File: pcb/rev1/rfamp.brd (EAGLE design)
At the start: 40 x 20 mm, 17 parts, among them IC1 TS520530, IC2 ADL5523, X1 SAW-B3721

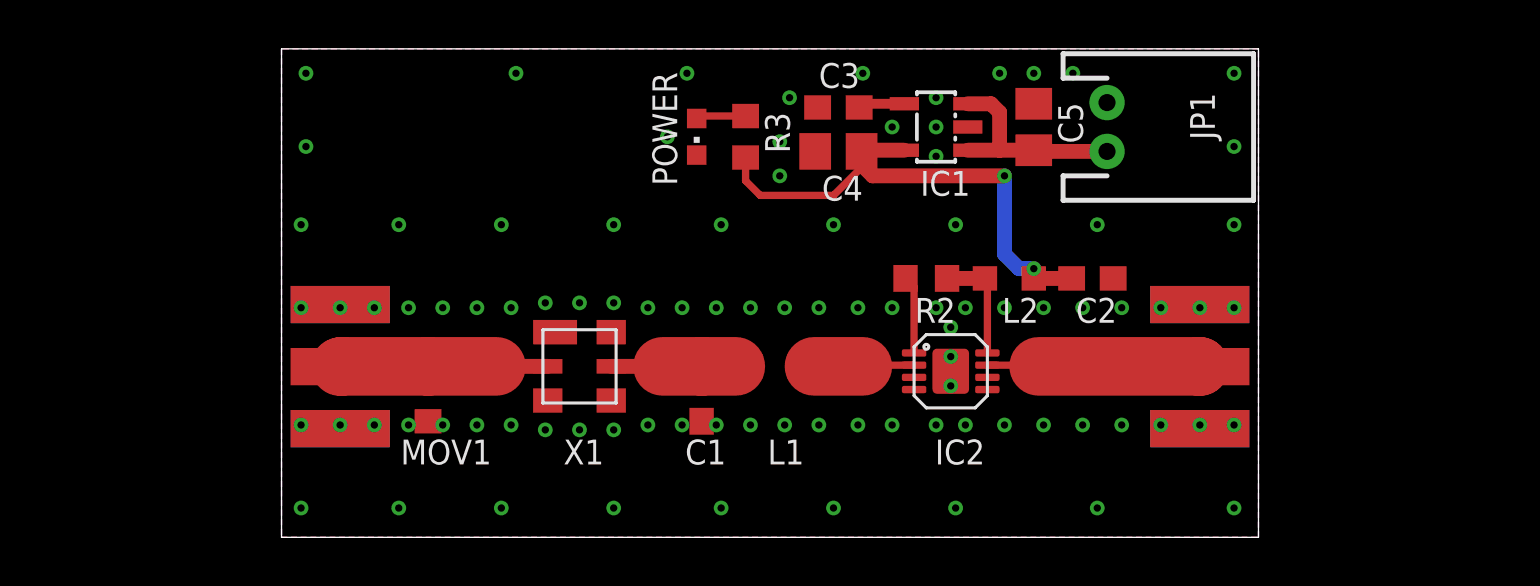
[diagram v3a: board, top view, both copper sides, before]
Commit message: Insert dc blocking capacitors.
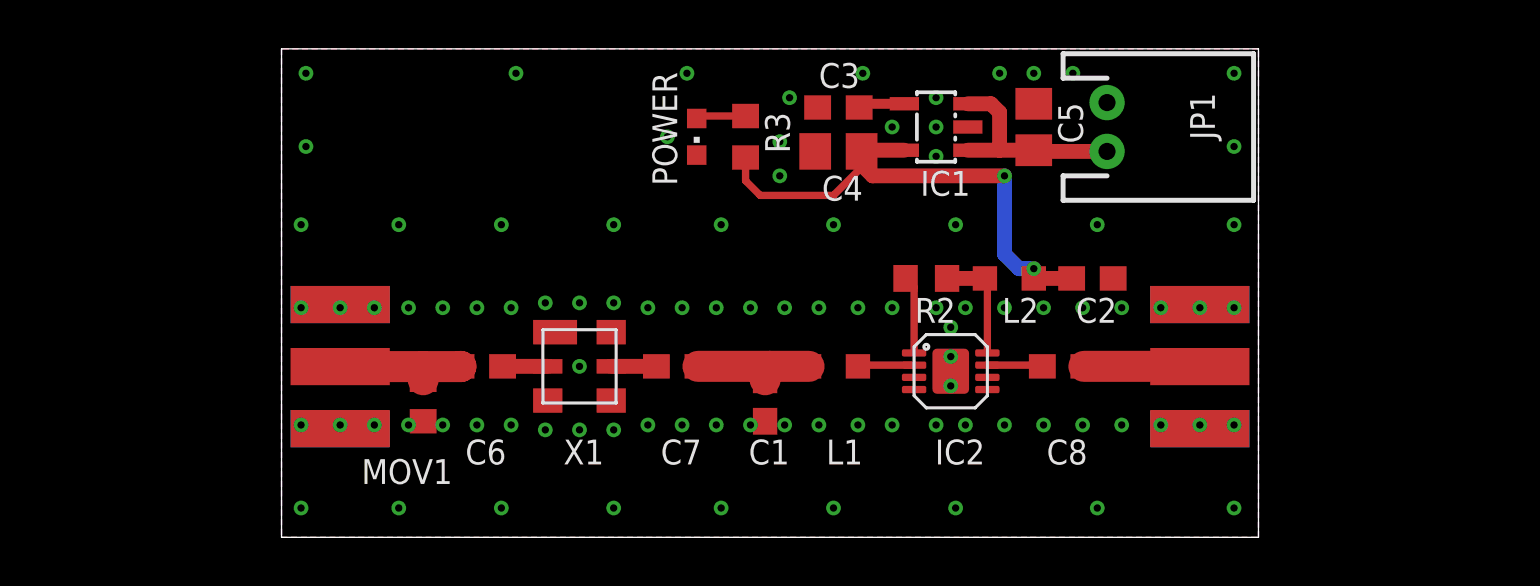
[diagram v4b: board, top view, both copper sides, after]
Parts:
- added C6, C7, C8: 100pF, rcl:C0603
- moved C1 2.60 mm to (19.8, 5.60)
- moved L1 2.40 mm to (22.6, 7.00)
- moved MOV1 0.20 mm to (5.80, 5.60)
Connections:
- new net N$10: C7.1, X1.5
- new net N$11: C8.2, J$2.SIG
- new net N$9: C6.2, X1.2
- net N$1: now also C6.1; no longer X1.2
- net N$2: now also C7.2; no longer X1.5
- net N$6: now also C8.1; no longer J$2.SIG
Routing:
- net N$6: track 8.72 -> 2.27 mm
- net GND: track 6.00 -> 12.0 mm, vias 93 -> 94
- net N$11: track 0.00 -> 4.75 mm
- net N$1: track 9.05 -> 5.49 mm
- net N$5: track 4.72 -> 2.32 mm
- net N$9: track 0.00 -> 1.85 mm
- net N$10: track 0.00 -> 1.85 mm
- net N$2: track 6.25 -> 5.18 mm
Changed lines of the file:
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@@
 <layer number="27" name="tValues" color="7" fill="1" visible="no" active="yes"/>
 <layer number="28" name="bValues" color="7" fill="1" visible="no" active="yes"/>
-<layer number="29" name="tStop" color="7" fill="3" visible="no" active="yes"/>
+<layer number="29" name="tStop" color="7" fill="3" visible="yes" active="yes"/>
 <layer number="30" name="bStop" color="7" fill="6" visible="no" active="yes"/>
 <layer number="31" name="tCream" color="7" fill="4" visible="no" active="yes"/>
@@
 <wire x1="0.8" y1="1.2" x2="39.2" y2="1.2" width="1.6" layer="29"/>
 <wire x1="0.8" y1="12.8" x2="39.2" y2="12.8" width="1.6" layer="29"/>
-<dimension x1="0" y1="0" x2="0" y2="20" x3="-12.4" y3="10" textsize="1.016" textratio="15" layer="48"/>
-<dimension x1="0" y1="20" x2="40" y2="20" x3="20" y3="24.8" textsize="1.016" textratio="15" layer="48"/>
+<dimension x1="0" y1="0" x2="0" y2="20" x3="-3.2" y3="10" textsize="1.016" textratio="15" layer="48"/>
+<dimension x1="0" y1="20" x2="40" y2="20" x3="20" y3="22.8" textsize="1.016" textratio="15" layer="48"/>
 <text x="39.4" y="15.6" size="1.016" layer="26" font="vector" ratio="15" rot="MR0">5V
 power</text>
 <text x="8.6" y="6.6" size="1.016" layer="26" font="vector" ratio="15" rot="MR0">RF input</text>
 <text x="38.2" y="6.6" size="1.016" layer="26" font="vector" ratio="15" rot="MR0">RF output</text>
+<polygon width="0.2" layer="41">
+<vertex x="0.2" y="8.8"/>
+<vertex x="11" y="8.8"/>
+<vertex x="11" y="5.2"/>
+<vertex x="0.2" y="5.2"/>
+</polygon>
+<polygon width="0.2" layer="41">
+<vertex x="13.4" y="8.8"/>
+<vertex x="25.6" y="8.8"/>
+<vertex x="25.6" y="5.2"/>
+<vertex x="13.4" y="5.2"/>
+</polygon>
+<polygon width="0.2" layer="41">
+<vertex x="29.2" y="8.8"/>
+<vertex x="39.6" y="8.8"/>
+<vertex x="39.6" y="5.2"/>
+<vertex x="29.2" y="5.2"/>
+</polygon>
 </plain>
 <attributes>
@@
 <attribute name="VALUE" x="13.2" y="10" size="1.016" layer="27" font="vector" ratio="15" rot="R90"/>
 </element>
-<element name="MOV1" library="rcl" package="R0603" value="" x="6" y="5.6" smashed="yes" rot="R90">
-<attribute name="NAME" x="8.6" y="4" size="1.016" layer="25" font="vector" ratio="15" rot="R180"/>
-<attribute name="VALUE" x="7.905" y="4.965" size="1.27" layer="27" rot="R90"/>
-</element>
-<element name="C1" library="rcl" package="C0603" value="NP" x="17.2" y="5.6" smashed="yes" rot="R270">
-<attribute name="NAME" x="18.2" y="4" size="1.016" layer="25" font="vector" ratio="15" rot="R180"/>
-<attribute name="VALUE" x="15.295" y="6.235" size="1.27" layer="27" rot="R270"/>
-</element>
-<element name="L1" library="rcl" package="L2012C" value="9nH" x="20.2" y="7" smashed="yes">
-<attribute name="NAME" x="21.4" y="4" size="1.016" layer="25" font="vector" ratio="15" rot="R180"/>
-<attribute name="VALUE" x="18.295" y="4.46" size="1.27" layer="27"/>
+<element name="MOV1" library="rcl" package="R0603" value="" x="5.8" y="5.6" smashed="yes" rot="R90">
+<attribute name="NAME" x="7" y="3.2" size="1.016" layer="25" font="vector" ratio="15" rot="R180"/>
+<attribute name="VALUE" x="7.705" y="4.965" size="1.27" layer="27" rot="R90"/>
+</element>
+<element name="C1" library="rcl" package="C0603" value="NP" x="19.8" y="5.6" smashed="yes" rot="R270">
+<attribute name="NAME" x="20.8" y="4" size="1.016" layer="25" font="vector" ratio="15" rot="R180"/>
+<attribute name="VALUE" x="17.895" y="6.235" size="1.27" layer="27" rot="R270"/>
+</element>
+<element name="L1" library="rcl" package="L2012C" value="9nH" x="22.6" y="7" smashed="yes">
+<attribute name="NAME" x="23.8" y="4" size="1.016" layer="25" font="vector" ratio="15" rot="R180"/>
+<attribute name="VALUE" x="20.695" y="4.46" size="1.27" layer="27"/>
 </element>
 <element name="R2" library="rcl" package="R0603" value="1K3" x="26.4" y="10.6" smashed="yes">
@@
 <element name="J$1" library="SparkFun" package="SMA-EDGE" value="SMA_EDGE" x="2.4" y="4.45" rot="R90"/>
 <element name="J$2" library="SparkFun" package="SMA-EDGE" value="SMA_EDGE" x="37.6" y="4.45" rot="R90"/>
+<element name="C6" library="rcl" package="C0603" value="100pF" x="8.2" y="7" smashed="yes">
+<attribute name="NAME" x="9.2" y="4" size="1.016" layer="25" font="vector" ratio="15" rot="R180"/>
+<attribute name="VALUE" x="7.565" y="5.095" size="1.27" layer="27"/>
+</element>
+<element name="C7" library="rcl" package="C0603" value="100pF" x="16.2" y="7" smashed="yes">
+<attribute name="NAME" x="17.2" y="4" size="1.016" layer="25" font="vector" ratio="15" rot="R180"/>
+<attribute name="VALUE" x="15.565" y="5.095" size="1.27" layer="27"/>
+</element>
+<element name="C8" library="rcl" package="C0603" value="100pF" x="32" y="7" smashed="yes">
+<attribute name="NAME" x="33" y="4" size="1.016" layer="25" font="vector" ratio="15" rot="R180"/>
+<attribute name="VALUE" x="31.365" y="5.095" size="1.27" layer="27"/>
+</element>
 </elements>
 <signals>
@@
 <via x="31.2" y="9.4" extent="1-16" drill="0.3"/>
 <via x="32.8" y="9.4" extent="1-16" drill="0.3"/>
-<via x="34.4" y="9.4" extent="1-16" drill="0.3"/>
 <via x="31.2" y="4.6" extent="1-16" drill="0.3"/>
 <via x="32.8" y="4.6" extent="1-16" drill="0.3"/>
-<via x="34.4" y="4.6" extent="1-16" drill="0.3"/>
-<via x="36" y="4.6" extent="1-16" drill="0.3"/>
-<via x="36" y="9.4" extent="1-16" drill="0.3"/>
 <via x="3.8" y="9.4" extent="1-16" drill="0.3"/>
 <via x="2.4" y="9.4" extent="1-16" drill="0.3"/>
@@
 <contactref element="J$2" pad="GND@1"/>
 <contactref element="J$2" pad="GND@0"/>
+<via x="12.2" y="7" extent="1-16" drill="0.3"/>
+<via x="34.4" y="9.4" extent="1-16" drill="0.3"/>
+<via x="34.4" y="4.6" extent="1-16" drill="0.3"/>
+<via x="36" y="4.6" extent="1-16" drill="0.3"/>
+<via x="37.6" y="4.6" extent="1-16" drill="0.3"/>
+<via x="39" y="4.6" extent="1-16" drill="0.3"/>
+<via x="36" y="9.4" extent="1-16" drill="0.3"/>
 <via x="37.6" y="9.4" extent="1-16" drill="0.3"/>
 <via x="39" y="9.4" extent="1-16" drill="0.3"/>
-<via x="37.6" y="4.6" extent="1-16" drill="0.3"/>
-<via x="39" y="4.6" extent="1-16" drill="0.3"/>
-</signal>
-<signal name="N$1" class="1">
+<wire x1="36" y1="9.4" x2="37.6" y2="9.4" width="0.3048" layer="1"/>
+<wire x1="37.6" y1="9.4" x2="39" y2="9.4" width="0.3048" layer="1"/>
+<wire x1="36" y1="4.6" x2="37.6" y2="4.6" width="0.3048" layer="1"/>
+<wire x1="37.6" y1="4.6" x2="39" y2="4.6" width="0.3048" layer="1"/>
+</signal>
+<signal name="N$1">
 <contactref element="MOV1" pad="2"/>
-<contactref element="X1" pad="2"/>
-<wire x1="6" y1="7" x2="8.8" y2="7" width="2.4" layer="1"/>
-<wire x1="8.8" y1="7" x2="10.9" y2="7" width="0.6096" layer="1"/>
-<wire x1="6" y1="6.45" x2="6" y2="7" width="0.6096" layer="1"/>
 <contactref element="J$1" pad="SIG"/>
-<wire x1="6" y1="7" x2="2.46" y2="7" width="2.4" layer="1"/>
-<wire x1="2.46" y1="7" x2="2.4" y2="6.99" width="2.4" layer="1"/>
-</signal>
-<signal name="N$2" class="1">
-<contactref element="X1" pad="5"/>
+<contactref element="C6" pad="1"/>
+<wire x1="2.4" y1="6.99" x2="5.8" y2="6.99" width="1.27" layer="1"/>
+<wire x1="5.8" y1="6.99" x2="7.34" y2="6.99" width="1.27" layer="1"/>
+<wire x1="7.34" y1="6.99" x2="7.35" y2="7" width="1.27" layer="1"/>
+<wire x1="5.8" y1="6.45" x2="5.8" y2="6.99" width="1.27" layer="1"/>
+</signal>
+<signal name="N$2">
 <contactref element="C1" pad="1"/>
 <contactref element="L1" pad="1"/>
-<wire x1="13.5" y1="7" x2="15.6" y2="7" width="0.6096" layer="1"/>
-<wire x1="15.6" y1="7" x2="17.2" y2="7" width="2.4" layer="1"/>
-<wire x1="17.2" y1="7" x2="18.6" y2="7" width="2.4" layer="1"/>
-<wire x1="18.6" y1="7" x2="19.2" y2="7" width="0.6096" layer="1"/>
-<wire x1="17.2" y1="6.45" x2="17.2" y2="7" width="0.6096" layer="1"/>
+<contactref element="C7" pad="2"/>
+<wire x1="21.6" y1="7" x2="20" y2="7" width="1.27" layer="1"/>
+<wire x1="20" y1="7" x2="17.05" y2="7" width="1.27" layer="1"/>
+<wire x1="19.8" y1="6.45" x2="19.8" y2="6.8" width="1.27" layer="1"/>
+<wire x1="19.8" y1="6.8" x2="20" y2="7" width="1.27" layer="1"/>
 </signal>
 <signal name="+3V3">
@@
 <wire x1="25.9" y1="10.25" x2="25.55" y2="10.6" width="0.3" layer="1"/>
 </signal>
-<signal name="N$5" class="1">
+<signal name="N$5">
 <contactref element="L1" pad="2"/>
 <contactref element="IC2" pad="2"/>
-<wire x1="21.2" y1="7" x2="21.8" y2="7" width="0.6096" layer="1"/>
-<wire x1="21.8" y1="7" x2="23.8" y2="7" width="2.4" layer="1"/>
-<wire x1="23.8" y1="7" x2="23.85" y2="7.05" width="0.3" layer="1"/>
-<wire x1="23.85" y1="7.05" x2="25.9" y2="7.05" width="0.3" layer="1"/>
-</signal>
-<signal name="N$6" class="1">
-<contactref element="IC2" pad="7"/>
-<wire x1="28.9" y1="7.05" x2="30.95" y2="7.05" width="0.3" layer="1"/>
-<wire x1="30.95" y1="7.05" x2="31" y2="7" width="0.3" layer="1"/>
-<contactref element="J$2" pad="SIG"/>
-<wire x1="31" y1="7" x2="37.59" y2="7" width="2.4" layer="1"/>
-<wire x1="37.59" y1="7" x2="37.6" y2="6.99" width="2.4" layer="1"/>
+<wire x1="25.9" y1="7.05" x2="23.65" y2="7.05" width="0.3048" layer="1"/>
+<wire x1="23.65" y1="7.05" x2="23.6" y2="7" width="0.3048" layer="1"/>
 </signal>
 <signal name="+5V">
@@
 <wire x1="17.1" y1="17.25" x2="17" y2="17.15" width="0.3" layer="1"/>
 </signal>
+<signal name="N$9">
+<contactref element="C6" pad="2"/>
+<contactref element="X1" pad="2"/>
+<wire x1="10.9" y1="7" x2="9.05" y2="7" width="0.6096" layer="1"/>
+</signal>
+<signal name="N$10">
+<contactref element="X1" pad="5"/>
+<contactref element="C7" pad="1"/>
+<wire x1="13.5" y1="7" x2="15.35" y2="7" width="0.6096" layer="1"/>
+</signal>
+<signal name="N$6">
+<contactref element="IC2" pad="7"/>
+<contactref element="C8" pad="1"/>
+<wire x1="28.9" y1="7.05" x2="31.1" y2="7.05" width="0.3048" layer="1"/>
+<wire x1="31.1" y1="7.05" x2="31.15" y2="7" width="0.3048" layer="1"/>
+</signal>
+<signal name="N$11">
+<contactref element="C8" pad="2"/>
+<contactref element="J$2" pad="SIG"/>
+<wire x1="32.85" y1="7" x2="37.59" y2="7" width="1.27" layer="1"/>
+<wire x1="37.59" y1="7" x2="37.6" y2="6.99" width="1.27" layer="1"/>
+</signal>
 </signals>

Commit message: Modified component values to match working prototype.
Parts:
- C3: value 100nF -> 22nF
- C4, C5: value 100nF -> 4.7uF
- IC1: value TS520530 -> NCP700BSN-30
- R2: value 1K3 -> 1K2
- R3: value 1K3 -> 390R
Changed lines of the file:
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@@
 <attribute name="VALUE" x="20.695" y="4.46" size="1.27" layer="27"/>
 </element>
-<element name="R2" library="rcl" package="R0603" value="1K3" x="26.4" y="10.6" smashed="yes">
+<element name="R2" library="rcl" package="R0603" value="1K2" x="26.4" y="10.6" smashed="yes">
 <attribute name="NAME" x="27.6" y="9.8" size="1.016" layer="25" font="vector" ratio="15" rot="R180"/>
 <attribute name="VALUE" x="25.765" y="8.695" size="1.27" layer="27"/>
@@
 <attribute name="VALUE" x="32.565" y="8.695" size="1.27" layer="27"/>
 </element>
-<element name="IC1" library="v-reg" package="SOT25" value="TS520530" x="26.8" y="16.8" smashed="yes" rot="R90">
+<element name="IC1" library="v-reg" package="SOT25" value="NCP700BSN-30" x="26.8" y="16.8" smashed="yes" rot="R90">
 <attribute name="NAME" x="28.2" y="15" size="1.016" layer="25" font="vector" ratio="15" rot="R180"/>
 <attribute name="VALUE" x="30.229" y="14.895" size="1.27" layer="27" rot="R90"/>
 </element>
-<element name="C3" library="rcl" package="C0603" value="100nF" x="22.8" y="17.6" smashed="yes" rot="R180">
+<element name="C3" library="rcl" package="C0603" value="22nF" x="22.8" y="17.6" smashed="yes" rot="R180">
 <attribute name="NAME" x="22" y="18.4" size="1.016" layer="25" font="vector" ratio="15"/>
 <attribute name="VALUE" x="23.435" y="19.505" size="1.27" layer="27" rot="R180"/>
 </element>
-<element name="C4" library="rcl" package="C0805" value="100nF" x="22.8" y="15.8" smashed="yes" rot="R180">
+<element name="C4" library="rcl" package="C0805" value="4.7uF" x="22.8" y="15.8" smashed="yes" rot="R180">
 <attribute name="NAME" x="23.8" y="14.8" size="1.016" layer="25" font="vector" ratio="15" rot="R180"/>
 <attribute name="VALUE" x="24.07" y="18.34" size="1.27" layer="27" rot="R180"/>
 </element>
-<element name="C5" library="rcl" package="C0805" value="100nF" x="30.8" y="16.8" smashed="yes" rot="R90">
+<element name="C5" library="rcl" package="C0805" value="4.7uF" x="30.8" y="16.8" smashed="yes" rot="R90">
 <attribute name="NAME" x="31.8" y="17.8" size="1.016" layer="25" font="vector" ratio="15" rot="R270"/>
 <attribute name="VALUE" x="33.34" y="15.53" size="1.27" layer="27" rot="R90"/>
@@
 <attribute name="VALUE" x="25.65" y="8.8" size="1.016" layer="27" font="vector" ratio="15"/>
 </element>
-<element name="R3" library="rcl" package="R0603" value="1K3" x="19" y="16.4" smashed="yes" rot="R90">
+<element name="R3" library="rcl" package="R0603" value="390R" x="19" y="16.4" smashed="yes" rot="R90">
 <attribute name="NAME" x="19.8" y="17.4" size="1.016" layer="25" font="vector" ratio="15" rot="R270"/>
 <attribute name="VALUE" x="20.905" y="15.765" size="1.27" layer="27" rot="R90"/>
